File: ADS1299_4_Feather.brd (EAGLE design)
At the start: 90 x 40 mm, 40 parts, among them U1 ADS1299-4PAG

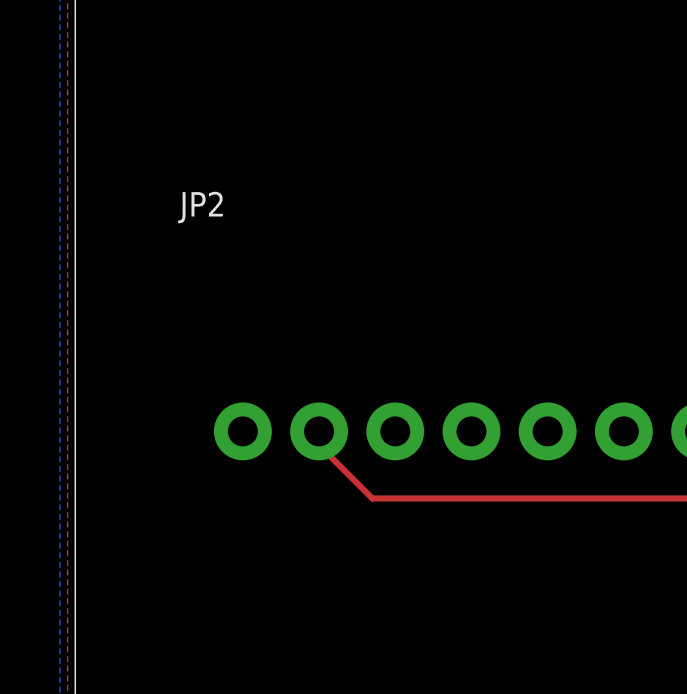
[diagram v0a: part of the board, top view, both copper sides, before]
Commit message: modified:   ADS1299_4_Feather.brd 		Moved soldermask layer to solder gerber group
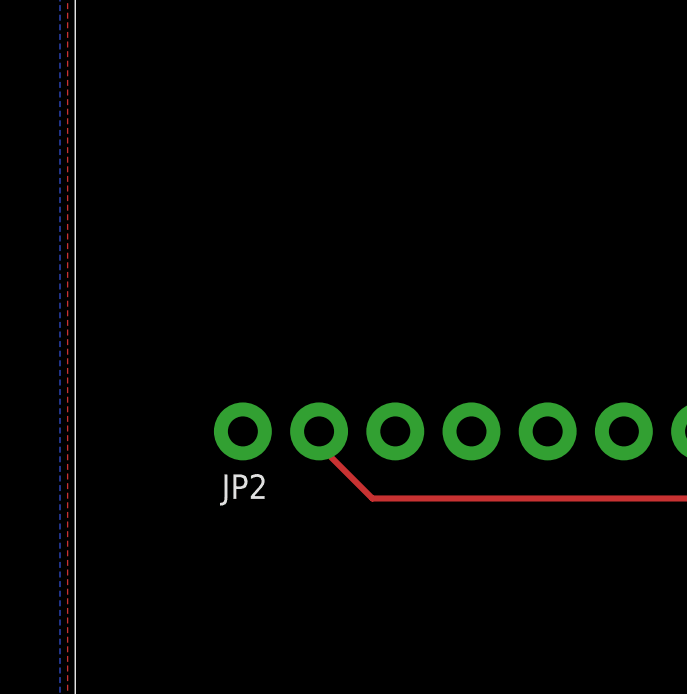
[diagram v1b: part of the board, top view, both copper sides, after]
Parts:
- moved FRAME1 0.30 mm to (0.14, 50.3)
